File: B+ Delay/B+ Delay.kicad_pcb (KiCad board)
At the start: 2 copper layers, 80 x 68 mm, 41 parts, among them J1 Pwr in, J2 B+ A, J3 B+ B, J4 LED, Q3 MMBT3904, Q4 MMBT3906, U1 LM7805_TO220, U2 SE556, U3 CPC1779, U4 CPC1779

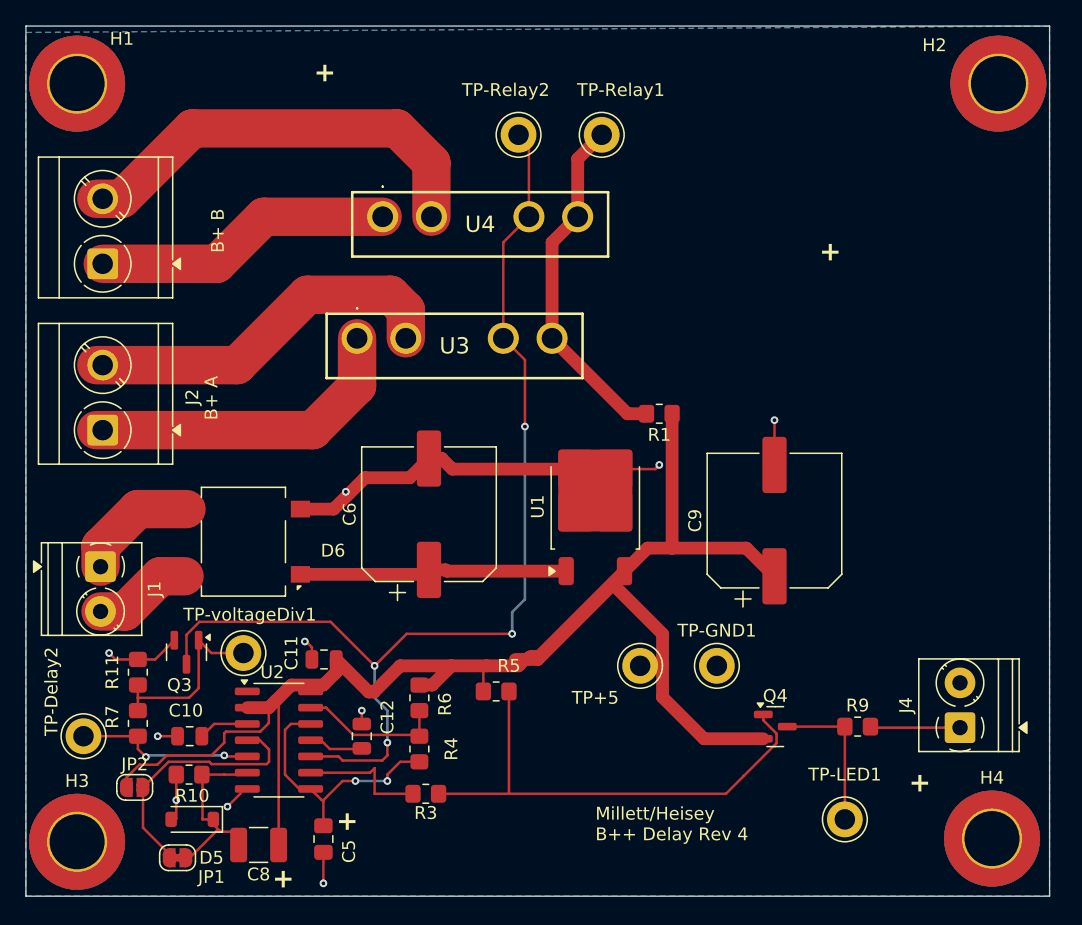
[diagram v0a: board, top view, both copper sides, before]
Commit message: Production batch
Putting one relay on top, another on bottom
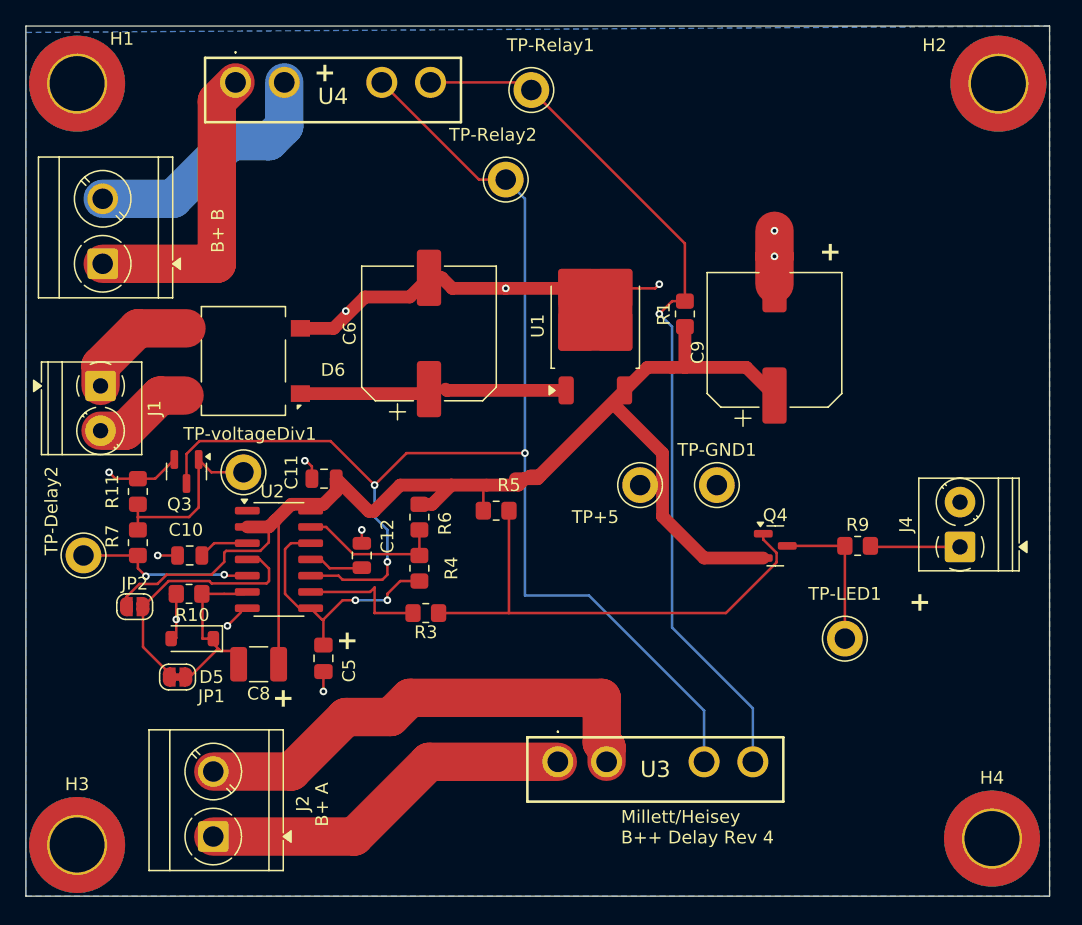
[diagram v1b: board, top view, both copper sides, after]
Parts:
- moved U3 36.6 mm to (191.6, -293.5)
- moved J2 32.9 mm to (164.6, -287.7)
- moved U4 15.6 mm to (166.4, -346.6)
- moved C10 14.1 mm to (162.8, -309.6)
- moved C11 14.1 mm to (173.3, -315.6)
- moved C12 14.1 mm to (176.2, -309.6)
- moved C5 14.1 mm to (173.2, -301.6)
- moved C6 14.1 mm to (181.5, -327.0)
- moved C8 14.1 mm to (168.2, -301.1)
- moved C9 14.1 mm to (208.5, -326.5)
- moved D5 14.1 mm to (163.0, -303.1)
- moved D6 14.1 mm to (167.0, -324.8)
- moved J1 14.1 mm to (155.8, -322.9)
- moved J4 14.1 mm to (223.0, -310.3)
- moved JP1 14.1 mm to (161.8, -300.1)
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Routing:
- net Net-(R1-Pad2): track 27.3 -> 70.0 mm, vias 0 -> 1
- net Net-(Q3-C): track 85.8 -> 113.0 mm, vias 4 -> 3
- net Net-(J3-Pin_2): track 33.8 -> 20.0 mm
- net A: track 29.2 -> 37.9 mm
- net +5V: track 123.1 -> 115.8 mm
- net Net-(J2-Pin_1): track 25.5 -> 29.3 mm
- net GND: track 45.7 -> 49.0 mm, vias 10 -> 12
- net Net-(D6-+): track 21.1 -> 19.8 mm

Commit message: Rev 5
Moved power supply parts so they don't bump SS relays, if they are bent over. Put 2nd relay so foil side is up for heatsink
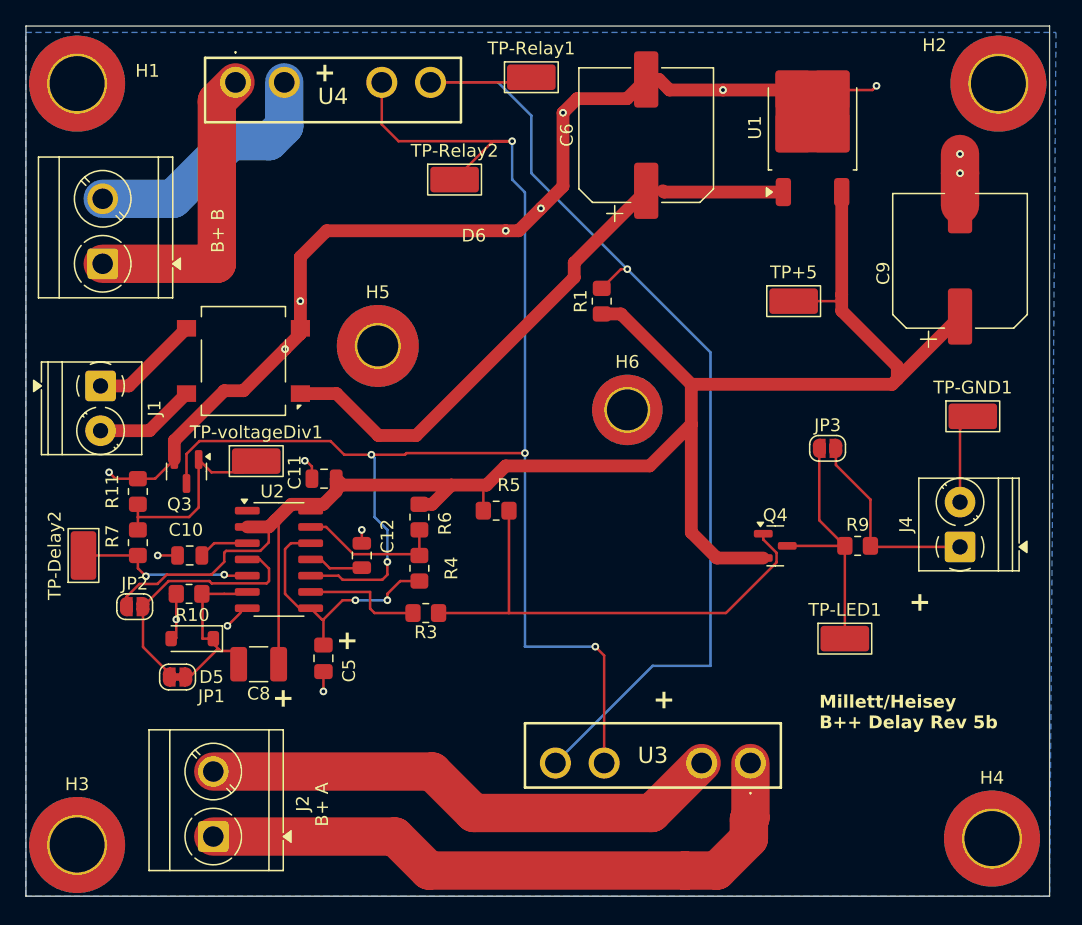
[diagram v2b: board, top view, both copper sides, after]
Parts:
- added H5: MountingHole, MountingHole:MountingHole_3.2mm_M3_Pad_TopBottom, F.Cu at (177.5, -326.0)
- added H6: MountingHole, MountingHole:MountingHole_3.2mm_M3_ISO14580_Pad_TopBottom, F.Cu at (197.0, -321.0)
- added JP3: Jumper_2_Open, Jumper:SolderJumper-2_P1.3mm_Open_RoundedPad1.0x1.5mm, F.Cu at (212.7, -318.0)
- TP+5, TP-Delay2, TP-GND1, TP-LED1, TP-Relay1, TP-Relay2, TP-voltageDiv1: footprint TestPoint:TestPoint_Keystone_5010-5014_Multipurpose -> TestPoint:TestPoint_Keystone_5019_Miniature
- moved C6 23.0 mm to (198.5, -342.5)
- moved U1 23.0 mm to (211.5, -343.1)
- moved TP-GND1 20.7 mm to (224.0, -320.5)
- moved TP+5 18.7 mm to (210.0, -329.5)
- moved C9 15.8 mm to (223.0, -332.6)
- moved U3 15.1 mm to (206.6, -293.4), turned to 180 degrees
- moved R1 6.58 mm to (195.0, -329.5)
- moved TP-Relay2 4.00 mm to (183.5, -339.0)
- moved TP-voltageDiv1 1.33 mm to (168.0, -317.0)
- moved TP-Relay1 1.00 mm to (189.5, -347.0)
- turned TP-Delay2 to 90 degrees
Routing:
- net GND: track 49.0 -> 101.1 mm, vias 12 -> 16
- net +5V: track 115.8 -> 143.1 mm
- net Net-(D6-+): track 19.8 -> 46.6 mm
- net Net-(J2-Pin_1): track 29.3 -> 49.9 mm
- net Net-(R1-Pad2): track 70.0 -> 82.9 mm
- net Net-(J4-Pin_1): track 0.00 -> 8.74 mm
- net Net-(JP3-A): track 11.4 -> 19.9 mm
- net Net-(Q3-C): track 113.0 -> 120.4 mm, vias 3 -> 5
- net A: track 37.9 -> 41.1 mm
- net Net-(J1-Pin_1): track 9.51 -> 8.58 mm
- net Net-(U2B-Q): track 7.14 -> 6.44 mm
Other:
- board text added: "Millett/Heisey B++ Delay Rev 5b"
- board text removed: "Millett/Heisey B++ Delay Rev 4"

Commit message: Moving terminal block over
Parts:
- moved J2 12.0 mm to (156.5, -296.4)
- moved C10 10.0 mm to (172.8, -309.0)
- moved C11 10.0 mm to (183.3, -315.0)
- moved C12 10.0 mm to (186.2, -309.0)
- moved C5 10.0 mm to (183.2, -301.0)
- moved C8 10.0 mm to (178.2, -300.5)
- moved D5 10.0 mm to (173.0, -302.5)
- moved JP1 10.0 mm to (171.8, -299.5)
- moved JP2 10.0 mm to (168.5, -305.0)
- moved Q3 10.0 mm to (172.6, -315.6)
- moved R10 10.0 mm to (172.8, -306.0)
- moved R11 10.0 mm to (168.8, -314.0)
- moved R3 10.0 mm to (191.2, -304.5)
- moved R4 10.0 mm to (190.8, -308.0)
- moved R5 10.0 mm to (196.8, -312.5)
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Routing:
- net Net-(Q3-C): track 120.4 -> 102.1 mm, vias 5 -> 4
- net Net-(J2-Pin_1): track 49.9 -> 63.1 mm
- net A: track 41.1 -> 54.2 mm
- net +5V: track 143.1 -> 133.3 mm
- net Net-(Q4-B): track 38.7 -> 29.0 mm
- net GND: track 101.1 -> 102.6 mm
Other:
- board text added: "Millett/Heisey B++ Delay Rev 5c"
- board text removed: "Millett/Heisey B++ Delay Rev 5b"

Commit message: Added 2 more time values w jumpers
default to 15s
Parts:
- removed JP1: ~, Jumper:SolderJumper-2_P1.3mm_Bridged_RoundedPad1.0x1.5mm
- removed JP2: ~, Jumper:SolderJumper-2_P1.3mm_Open_RoundedPad1.0x1.5mm
- added JP1_15S1: , Jumper:SolderJumper-2_P1.3mm_Bridged_Pad1.0x1.5mm, F.Cu at (161.0, -315.4)
- added JP2_30s1: Jumper_2_Open, Jumper:SolderJumper-2_P1.3mm_Open_RoundedPad1.0x1.5mm, F.Cu at (161.5, -311.4)
- added JP3_30s1: Jumper_2_Open, Jumper:SolderJumper-2_P1.3mm_Open_RoundedPad1.0x1.5mm, F.Cu at (156.0, -308.4)
- added R12: 2M, Resistor_SMD:R_0805_2012Metric_Pad1.20x1.40mm_HandSolder, F.Cu at (168.5, -304.5)
- added R13: 3.3M, Resistor_SMD:R_0805_2012Metric_Pad1.20x1.40mm_HandSolder, F.Cu at (168.5, -299.6)
- moved TP-Delay2 11.4 mm to (154.0, -313.5)
- moved R10 0.25 mm to (172.5, -306.0)
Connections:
- R10 pad 2: GND -> Net-(JP1_15S1-B)
- U2 pad 4: Net-(JP1-B) -> +5V
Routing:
- net Net-(JP1-B): track 20.3 -> 0.00 mm
- net Net-(JP3_30s1-B): track 0.00 -> 19.3 mm
- net Net-(JP1_15S1-B): track 0.00 -> 15.4 mm
- net Net-(U2A-Q): track 14.3 -> 26.7 mm
- net Net-(JP2_30s1-B): track 0.00 -> 11.7 mm
- net +5V: track 133.3 -> 121.8 mm
- net GND: track 102.6 -> 111.6 mm, vias 16 -> 17
- net Net-(D5-K): track 13.7 -> 19.7 mm
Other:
- board text added: "Millett/Heisey B++ Delay Rev 5d"
- board text removed: "Millett/Heisey B++ Delay Rev 5c"

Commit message: Made 60s default
Jumpers for 45s and 15s
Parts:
- removed JP1_15S1: , Jumper:SolderJumper-2_P1.3mm_Bridged_Pad1.0x1.5mm
- removed JP2_30s1, JP3_30s1: Jumper_2_Open, Jumper:SolderJumper-2_P1.3mm_Open_RoundedPad1.0x1.5mm
- added JP1: 15 sec, Jumper:SolderJumper-2_P1.3mm_Open_RoundedPad1.0x1.5mm, F.Cu at (159.0, -308.9)
- added JP2: 45s, Jumper:SolderJumper-2_P1.3mm_Open_RoundedPad1.0x1.5mm, F.Cu at (164.2, -306.0)
- added JP4: Jumper_2_Open, Jumper:SolderJumper-2_P1.3mm_Open_RoundedPad1.0x1.5mm, F.Cu at (212.5, -318.0)
- JP3: value Jumper_2_Open -> 60sec; footprint Jumper:SolderJumper-2_P1.3mm_Open_RoundedPad1.0x1.5mm -> Jumper:SolderJumper-2_P1.3mm_Bridged_Pad1.0x1.5mm
- moved JP3 50.2 mm to (165.0, -302.4), turned to -90 degrees
- moved R13 1.45 mm to (167.5, -298.5), turned to 180 degrees
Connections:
- JP3 pad 1: Net-(JP3-A) -> GND
- JP3 pad 2: Net-(J4-Pin_1) -> Net-(JP3-B)
- Q4 pad 3: Net-(JP3-A) -> Net-(JP4-A)
- R13 pad 2: Net-(JP3_30s1-B) -> Net-(JP3-B)
- R9 pad 1: Net-(JP3-A) -> Net-(JP4-A)
- TP-LED1 pad 1: Net-(JP3-A) -> Net-(JP4-A)
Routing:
- net Net-(JP4-A): track 0.00 -> 19.9 mm
- net Net-(JP3-A): track 19.9 -> 0.00 mm
- net Net-(JP3_30s1-B): track 19.3 -> 0.00 mm
- net Net-(JP2-B): track 11.7 -> 3.35 mm
- net GND: track 111.6 -> 107.6 mm, vias 17 -> 18
- net Net-(JP3-B): track 0.00 -> 3.82 mm
- net Net-(D5-K): track 19.7 -> 21.8 mm
- net Net-(JP1-B): track 15.4 -> 13.7 mm

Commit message: Latest production build
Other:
- board text added: "Millett/Heisey B++ Delay Rev 5e"
- board text removed: "Millett/Heisey B++ Delay Rev 5d"
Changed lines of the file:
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@@
 		(property "Value" "15 sec"
 			(at 0 1.9 90)
-			(layer "F.Fab")
+			(layer "F.SilkS")
 			(effects
 				(font
@@
 		(property "Value" "60sec"
 			(at 0 1.9 90)
-			(layer "F.Fab")
+			(layer "F.SilkS")
 			(effects
 				(font
@@
 		(property "Value" "45s"
 			(at -3.15 -0.5 0)
-			(layer "F.Fab")
+			(layer "F.SilkS")
 			(effects
 				(font
@@
 	)
 	(gr_text "+"
+		(at 179 -297 0)
+		(layer "F.SilkS")
+		(effects
+			(font
+				(size 1.5 1.5)
+				(thickness 0.3)
+				(bold yes)
+			)
+			(justify left bottom)
+		)
+	)
+	(gr_text "+"
 		(at 172.5 -346.5 0)
 		(layer "F.SilkS")
@@
 		)
 	)
-	(gr_text "Millett/Heisey\nB++ Delay Rev 5d"
+	(gr_text "Millett/Heisey\nB++ Delay Rev 5e"
 		(at 212 -296 0)
 		(layer "F.SilkS")
@@
 	)
 	(gr_text "+"
-		(at 199 -297.5 0)
+		(at 199 -289.5 0)
 		(layer "F.SilkS")
 		(effects
